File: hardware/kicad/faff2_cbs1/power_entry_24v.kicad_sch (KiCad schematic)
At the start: 28 parts, among them J201 KPJX-4S, Q201 DMP6023LFG-7

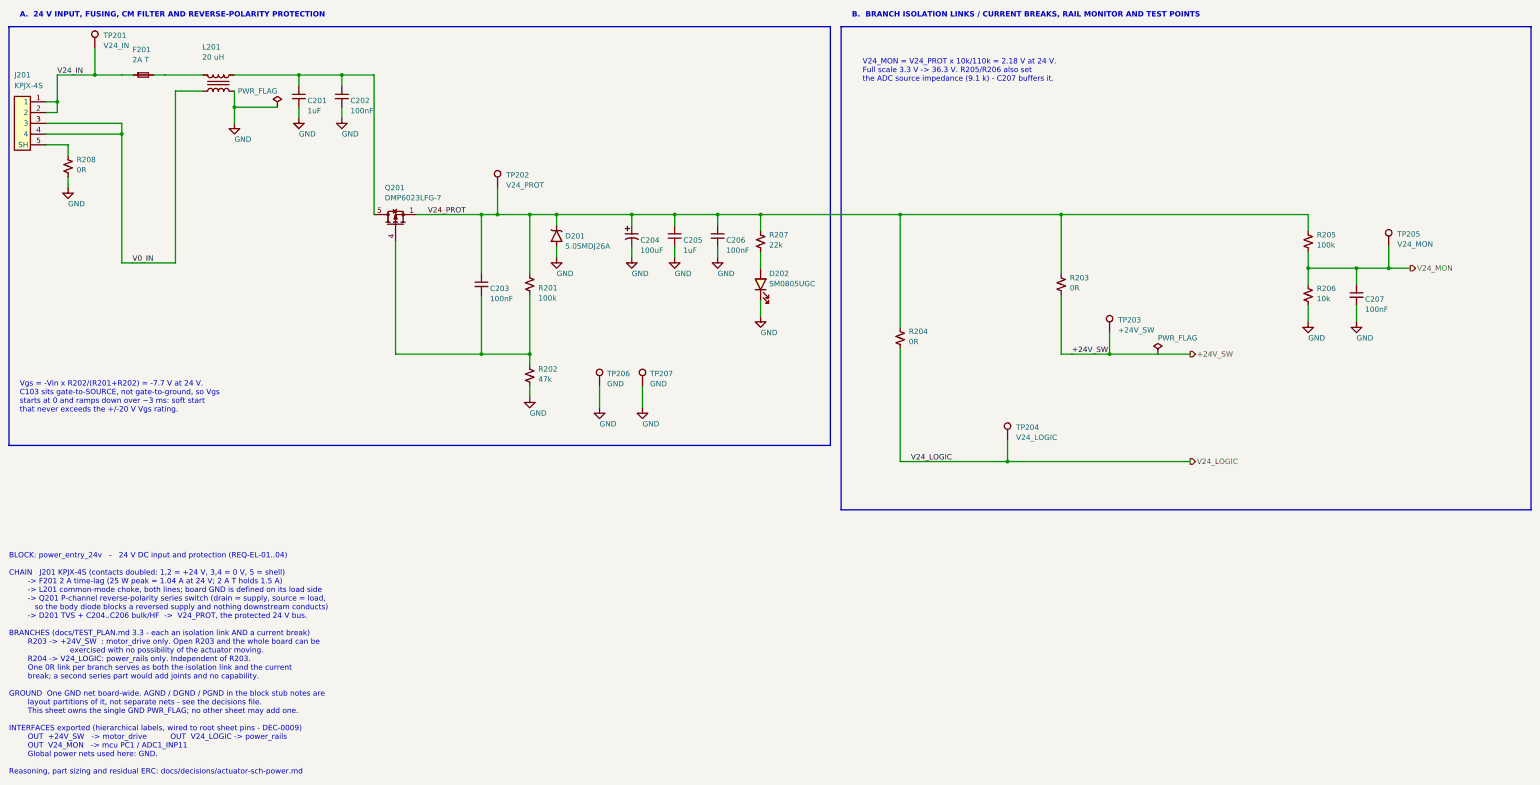
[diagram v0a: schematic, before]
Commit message: review r1 final sweep: power labels, TP silkscreen names, text overlaps
The captain's design-wide pass, run once the per-sheet batches had landed.
Presentation only: ERC 0 errors / 0 warnings at severity-all, 404 components,
251 nets, and every per-net node set identical to the pre-sweep export.

  power labels   92 rail names were hidden on loadcell_afe, motor_drive and
                 temp_sense - all 285 power symbols now read, placed to the
                 house pattern (GND below the symbol, rail arrows above)
  test points    66 of 83 still carried the library default "TestPoint". All
                 83 now name what they measure, from the net they actually
                 land on in the netlist; longest is 5 characters
  text overlap   16 collisions cleared design-wide, four of them sub-millimetre
                 ones the bundled checker passes because it under-measures text
  GND upside down  none - 0 of 285 power symbols is rotated or mirrored
  graphic/wire   one: power_rails block D's bottom border lay along the last
                 PWR_FLAG's wire; the flag column moved up 2.54

The overlap checker turns out to have three separable blind spots, each settled
here by measuring a render rather than by reading the format: it grows every
text field rightward regardless of justify/mirror/180-rotation, so its box is a
mirror image of the truth for those and it both invents and misses collisions;
it measures text at ~1.06 mm per character where the real advance is ~1.19; and
it reflects a rotated symbol's body about the origin. tools/sch_geom.py models
all three correctly and the design is clean under it design-wide. Two of that
model's own rules - notes growing up from their anchor, and labels taking no
180-degree justify flip - were bugs of mine that the checker caught first. The
render is what settles it; neither tool is authoritative alone.

Placement is searched rather than guessed: 177 newly visible fields are tried
against every wire, block border, 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
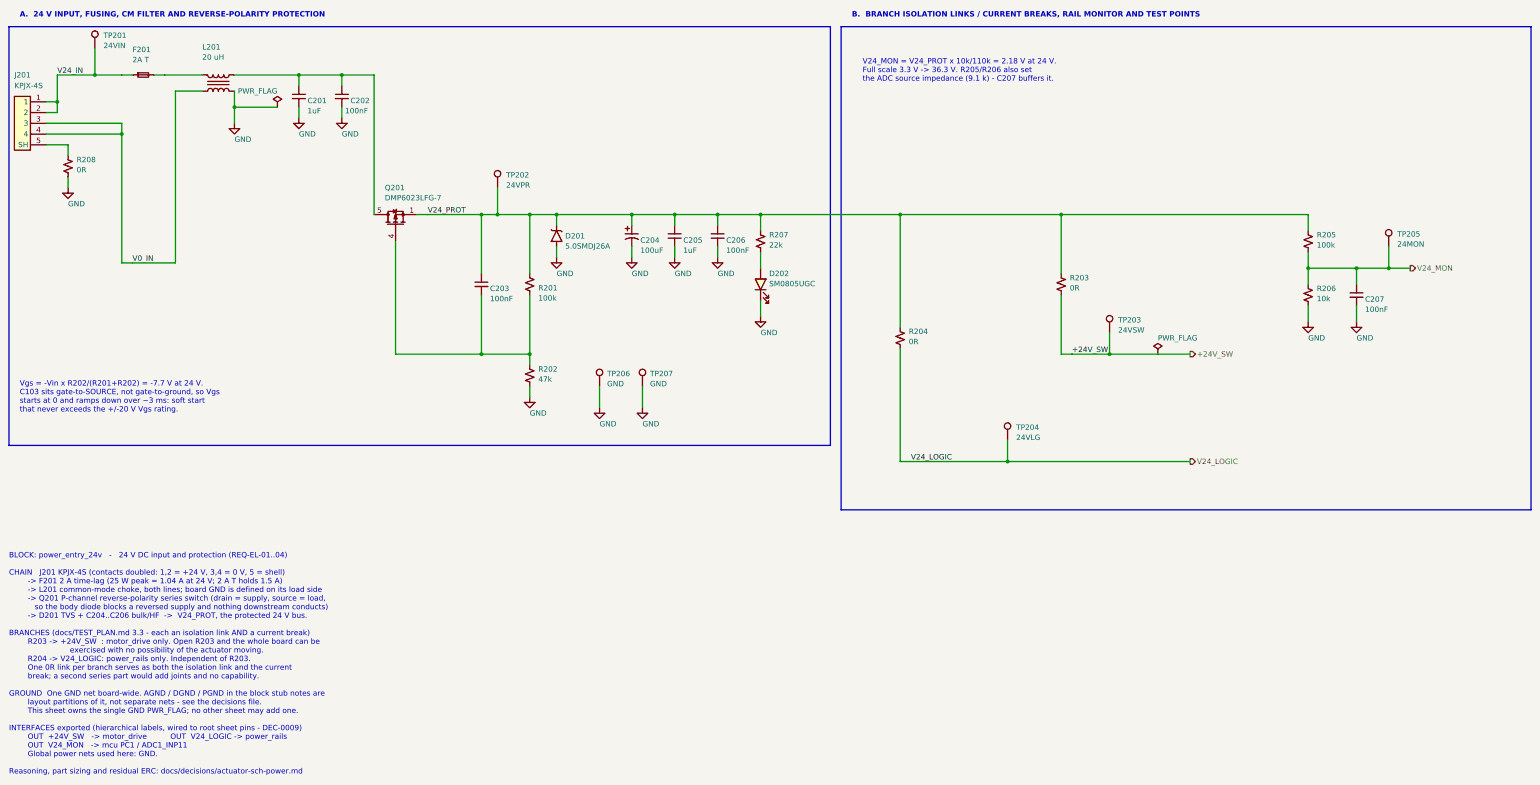
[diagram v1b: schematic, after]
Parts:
- TP201: value V24_IN -> 24VIN
- TP202: value V24_PROT -> 24VPR
- TP203: value +24V_SW -> 24VSW
- TP204: value V24_LOGIC -> 24VLG
- TP205: value V24_MON -> 24MON
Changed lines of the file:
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@@
 		)
 		(property "Value" "100nF"
-			(at 98.55 46.58 0)
+			(at 97.28 46.58 0)
 			(effects
 				(font
@@
 			)
 		)
-		(property "Value" "V24_IN"
+		(property "Value" "24VIN"
 			(at 40.13 31.15 0)
 			(effects
@@
 			)
 		)
-		(property "Value" "V24_PROT"
+		(property "Value" "24VPR"
 			(at 135.38 64.17 0)
 			(effects
@@
 			)
 		)
-		(property "Value" "V24_LOGIC"
+		(property "Value" "24VLG"
 			(at 256.03 123.86 0)
 			(effects
@@
 			)
 		)
-		(property "Value" "+24V_SW"
+		(property "Value" "24VSW"
 			(at 280.16 98.46 0)
 			(effects
@@
 			)
 		)
-		(property "Value" "V24_MON"
+		(property "Value" "24MON"
 			(at 346.2 78.14 0)
 			(effects

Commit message: review r2 item 8: one placement rule for every power symbol's net name
"Directly above it, centre justified, and close" - applied as no sideways
offset, centred, 3.81 mm away: above a rail arrow, below a ground. All 283
power symbols now carry it; 103 did not, most left-anchored rather than centred
and a few offset up to 7.6 mm sideways by round 1's auto-placer.

The ground mirror is an interpretation and is flagged as such: "above" a GND
symbol is where its wire arrives, and 137 instances plus every convention put
GND's name under the triangle. One line to change if the captain meant it
literally.

What makes this different from round 1 is that the label is now PINNED, so
everything else moves instead - the symbol along its own stub, a note to the
nearest clear spot, a block box outward (five rectangles grew where a name sat
on a border with clear space beyond), and two PWR_FLAGs placed by hand because
their 9.5 mm names do not fit the 10 mm rail runs they tap.

Thirteen of 283 still graze a wire, body or note on the two densest sheets and
are listed in the decisions file rather than hidden. Each needs the parts around
it respaced, which is more than a label sweep should do unasked - the TIM1 note
on motor_drive in particular has nowhere to go: no clear position exists for a
47.6 x 8.7 mm box anywhere in that block.

Also recorded: my own severity metric scored wire-through-text at zero for a
while, because a wire is a zero-thickness segment and box-intersection depth
against it is always 0. For those, severity is how far inside the box the line
sits. A render caught it; the number did not.

ERC 0 errors / 0 warnings at severity-all; 412 components, 259 nets, node sets
identical to before the batch. Review PDF regenerated once, here, for the whole
of round 2.

Co-Authored-By: Claude Opus 5 <noreply@anthropic.com>
Claude-Session: https://claude.ai/code/session_01PFWfwT8RZc8Zqn8vgZxV8j
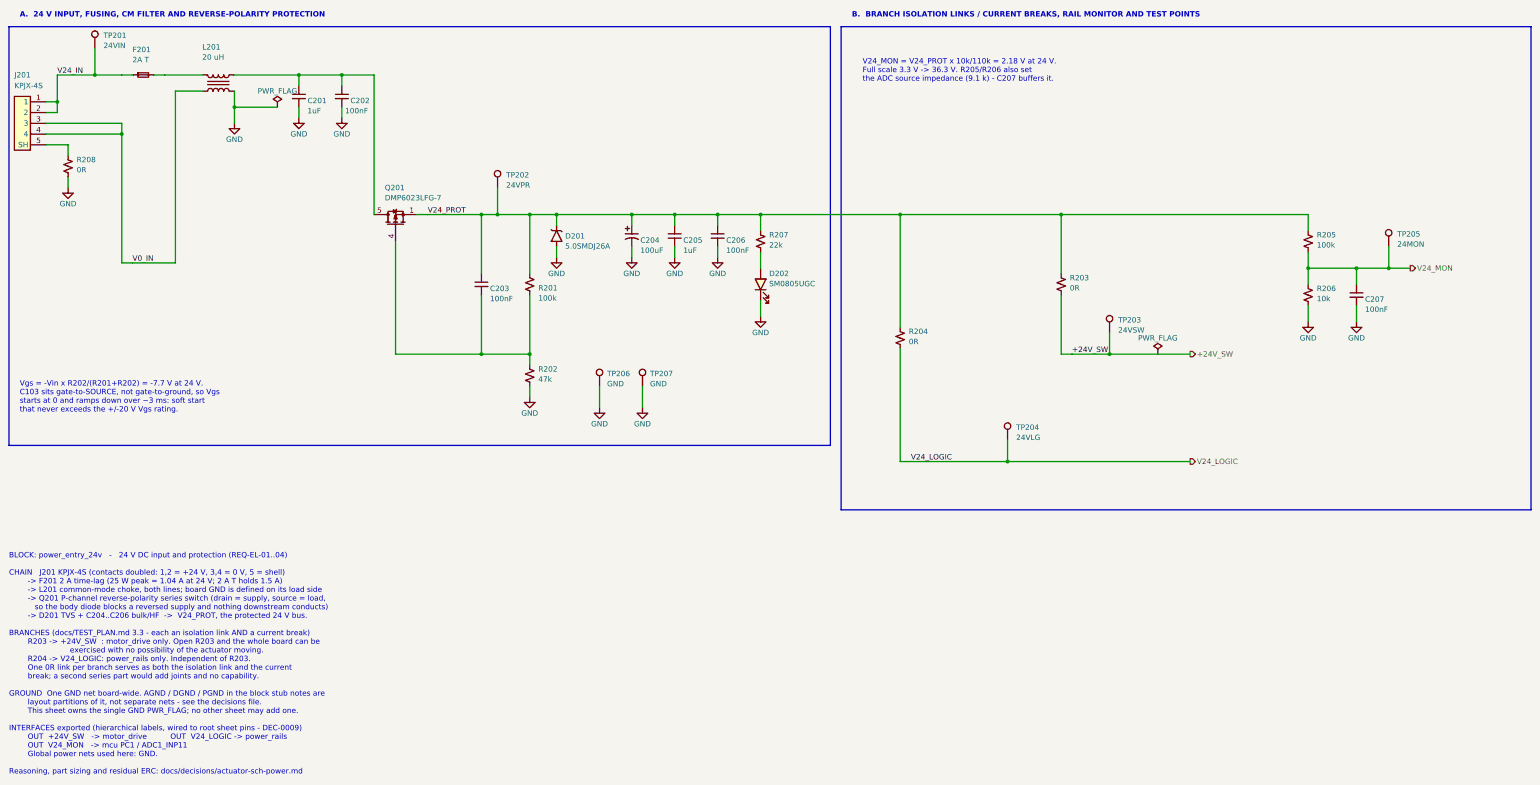
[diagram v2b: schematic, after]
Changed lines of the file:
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@@
 					(size 1.27 1.27)
 				)
-				(justify left)
 			)
 		)
@@
 					(size 1.27 1.27)
 				)
-				(justify left)
 			)
 		)
@@
 					(size 1.27 1.27)
 				)
-				(justify right)
 			)
 		)
@@
 					(size 1.27 1.27)
 				)
-				(justify left)
 			)
 		)
@@
 					(size 1.27 1.27)
 				)
-				(justify left)
 			)
 		)
@@
 					(size 1.27 1.27)
 				)
-				(justify left)
 			)
 		)
@@
 					(size 1.27 1.27)
 				)
-				(justify left)
 			)
 		)
@@
 					(size 1.27 1.27)
 				)
-				(justify left)
 			)
 		)
@@
 					(size 1.27 1.27)
 				)
-				(justify left)
 			)
 		)
@@
 					(size 1.27 1.27)
 				)
-				(justify left)
 			)
 		)
@@
 					(size 1.27 1.27)
 				)
-				(justify left)
 			)
 		)
@@
 					(size 1.27 1.27)
 				)
-				(justify left)
 			)
 		)
@@
 					(size 1.27 1.27)
 				)
-				(justify left)
 			)
 		)
@@
 					(size 1.27 1.27)
 				)
-				(justify left)
 			)
 		)
@@
 					(size 1.27 1.27)
 				)
-				(justify left)
 			)
 		)
@@
 					(size 1.27 1.27)
 				)
-				(justify left)
 			)
 		)
